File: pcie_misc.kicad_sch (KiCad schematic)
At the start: 0 parts

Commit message: [#57056] Add PCIe circuitry
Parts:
- added C53: C_22u_0603, antmicro-footprints:C_0603_1608Metric, symbol antmicroCapacitors0603:C_22u_0603
- added C54, C55, C56, C57, C58, C60: C_100n_0402, antmicro-footprints:C_0402_1005Metric, symbol antmicroCapacitors0402:C_100n_0402
- added C59: C_68n_0402, antmicro-footprints:C_0402_1005Metric, symbol antmicroCapacitors0402:C_68n_0402
- added R35, R36, R37, R38, R39, R40, R41, R42, R43, R44, R45, R46: R_0R_0402, antmicro-footprints:R_0402_1005Metric, symbol antmicroResistors0402:R_0R_0402
- added R47, R48, R49, R50, R51, R52, R53, R54, R55, R56, R57: R_1k_0402, antmicro-footprints:R_0402_1005Metric, symbol antmicroResistors0402:R_1k_0402
- added TP1, TP2, TP3, TP4: TP_0.75mm_SMD, antmicro-footprints:TP_SMD_0.75mm, symbol antmicroTestPoints:TP_0.75mm_SMD
- added U1: 9DBL0651CKILF, antmicro-footprints:UQFN-40-1EP_5x5mm_P0.4mm_EP3.8x3.8mm, symbol antmicroClockTimingClockGeneratorsPLLsFrequencySynthesizers:9DBL0651CKILF
- added U2: 74AUP2G132, antmicro-footprints:VSSOP-8_2.3x2mm_P0.5mm, symbol antmicroLogicGatesandInverters:74AUP2G132
- added U3: TPS3840PL30DBVR, antmicro-footprints:SOT-23-5, symbol antmicroPMICPowerSequencers:TPS3840PL30DBVR
- added Y1: Oscillator_32.768kHz_ECS_2520MV, antmicro-footprints:Oscillator_SMD_ECS_2520MV_2.5x2mm, symbol antmicroOscillators:Oscillator_32.768kHz_ECS_2520MV
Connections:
- new net: C59.2, C60.2, U3.5 (CT)
- new net: R52.1, U1.38 (~{OE5})
- new net: R56.1, Y1.1 (EN)
- new net: R54.2, R55.1, U1.2 (~{HIBW_BYPM_LOBW})
- new net: R47.1, U1.13 (~{OE0})
- new net: TP4.1, U3.4 (~{MR})
- new net: R50.1, U1.29 (~{OE3})
- new net: R48.1, U1.21 (~{OE1})
- new net: TP3.1, U1.1 (SADR_{TRI})
- new net: TP2.1, U1.10 (SDAT)
- new net: R49.1, U1.24 (~{OE2})
- new net: R51.1, U1.35 (~{OE4})
- new net: R53.1, U1.40 (~{CKPWRGD_PD})
- new net: TP1.1, U1.9 (SCLK)
- new net: U2.1 (1A), U2.2 (1B), Y1.3 (OUT)
- new net +3V3: C53.2, C54.2, C55.2, C56.2, C57.2, C58.2, R52.2, R53.2, R54.1, R56.2, R57.2, U1.11 (VDDDIG3V3), U1.12 (VDDIO), U1.16 (VDD3V3), U1.17 (VDDIO), U1.25 (VDDA3V3), U1.26 (VDDIO), U1.31 (VDD3V3), U1.32 (VDDIO), U1.39 (VDDIO), U1.5 (VDDR), U2.8 (VCC), U3.2 (VDD), Y1.4 (VDD)
- new net DIF0+: R35.1, U1.14 (DIF0+)
- new net DIF0-: R36.1, U1.15 (DIF0-)
- new net DIF1+: R37.1, U1.18 (DIF1+)
- new net DIF1-: R38.1, U1.19 (DIF1-)
- new net DIF2+: R39.1, U1.22 (DIF2+)
- new net DIF2-: R40.1, U1.23 (DIF2-)
- new net DIF3+: R41.1, U1.27 (DIF3+)
- new net DIF3-: R42.1, U1.28 (DIF3-)
- new net DIF4+: R43.1, U1.33 (DIF4+)
- new net DIF4-: R44.1, U1.34 (DIF4-)
- new net DIF5+: R45.1, U1.36 (DIF5+)
- new net DIF5-: R46.1, U1.37 (DIF5-)
- new net GND: C53.1, C54.1, C55.1, C56.1, C57.1, C58.1, C59.1, C60.1, R47.2, R48.2, R49.2, R50.2, R51.2, R55.2, U1.41 (EPAD), U1.8 (GNDDIG), U2.4 (GND), U2.5 (2A), U2.6 (2B), U3.3 (GND), Y1.2 (GND)
- new net PCIE_{REF0}.CK+: R35.2
- new net PCIE_{REF0}.CK-: R36.2
- new net PCIE_{REF1}.CK+: R37.2
- new net PCIE_{REF1}.CK-: R38.2
- new net PCIE_{REF2}.CK+: R39.2
- new net PCIE_{REF2}.CK-: R40.2
- new net PCIE_{REF3}.CK+: R41.2
- new net PCIE_{REF3}.CK-: R42.2
- new net PCIE_{REF4}.CK+: R43.2
- new net PCIE_{REF4}.CK-: R44.2
- new net PCIE_{REFIN}.CK+: U1.6 (CLK_IN+)
- new net PCIE_{REFIN}.CK-: U1.7 (CLK_IN-)
- new net SUSCLK: U2.7 (1Y)
- new net ~{PERST}: R57.1, U3.1 (~{RESET})
- no-connect marks 0 -> 3
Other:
- note added: "100 ms delay"
- note added: "PCIe CLOCK FANOUT BUFFER"
- note added: "SUSCLK generator"
- note added: "~{PERST} generator"
- company: (none) -> Antmicro Ltd.
- title: (none) -> Com Express 7 baseboard

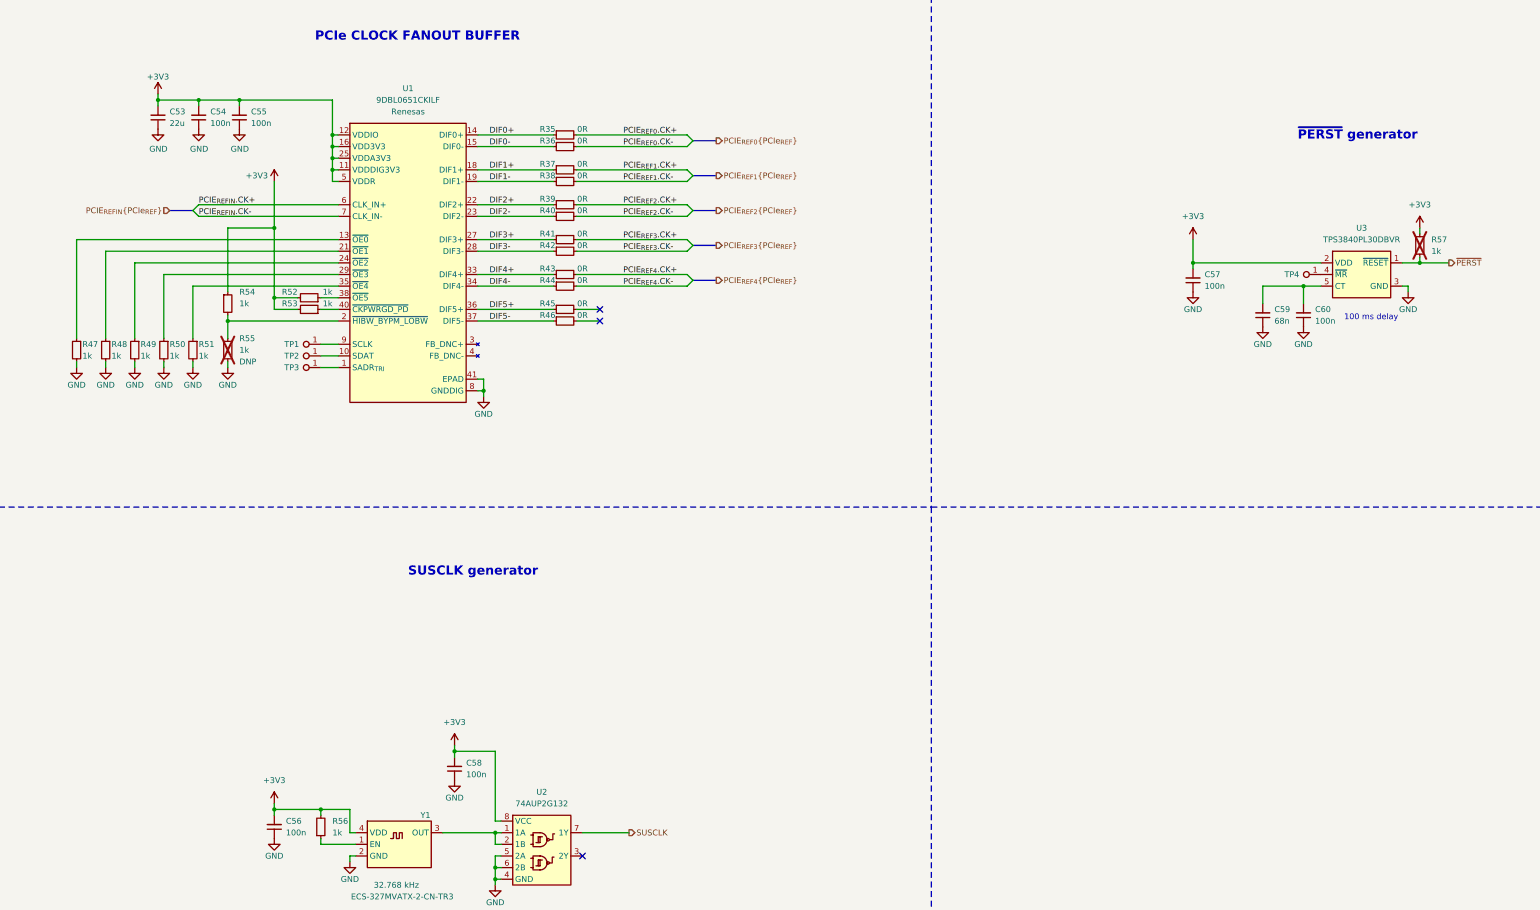
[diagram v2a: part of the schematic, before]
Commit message: [#58137] Update backplane connector pinout
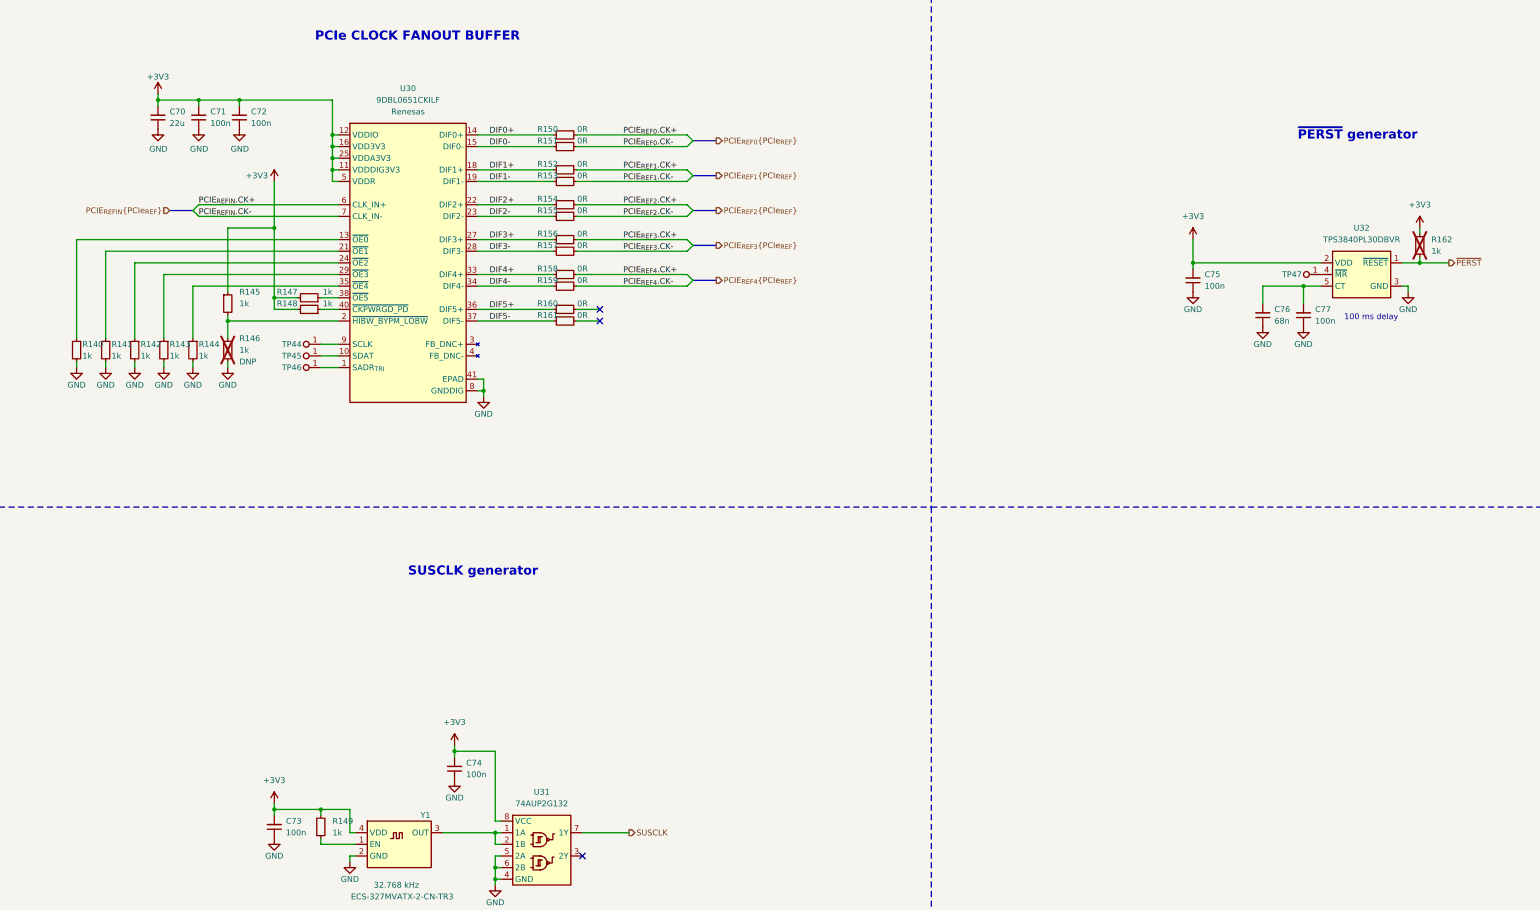
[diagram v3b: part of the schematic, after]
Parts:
- renumbered C53 to C70, C54 to C71, C55 to C72, C56 to C73, C58 to C74, C57 to C75, C59 to C76, C60 to C77, R47 to R140, R48 to R141, R49 to R142, R50 to R143, R51 to R144, R54 to R145, R55 to R146, R52 to R147, R53 to R148, R56 to R149, R35 to R150, R36 to R151, R37 to R152, R38 to R153, R39 to R154, R40 to R155, R41 to R156, R42 to R157, R43 to R158, R44 to R159, R45 to R160, R46 to R161, R57 to R162, TP1 to TP44, TP2 to TP45, TP3 to TP46, TP4 to TP47, U1 to U30, U2 to U31, U3 to U32

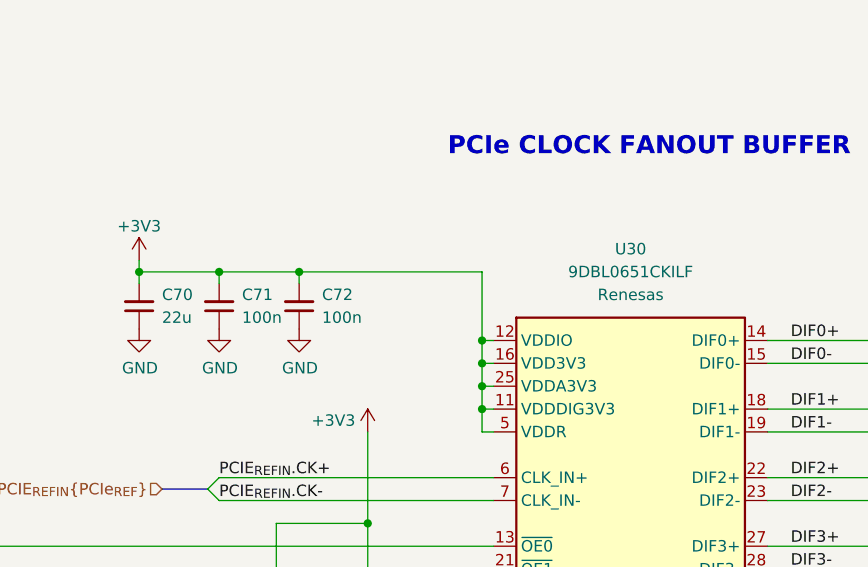
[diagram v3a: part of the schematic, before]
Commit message: [#58137] Add DC/DC supplies
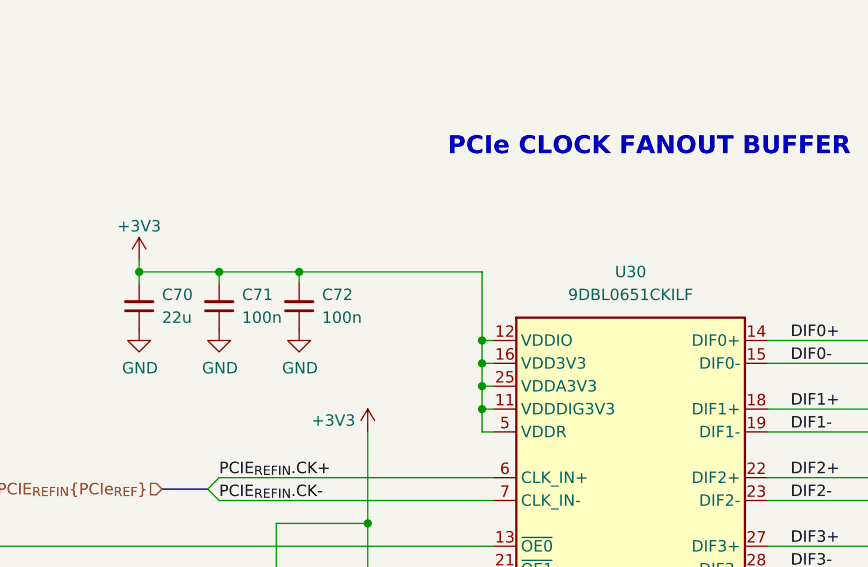
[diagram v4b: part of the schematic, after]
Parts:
- C70: value C_22u_0603 -> C_22u_16V_0603; symbol antmicroCapacitors0603:C_22u_0603 -> antmicroCapacitors0603:C_22u_16V_0603; MPN GRM188R60J226MEA0D -> CL10A226MO7JZNC; Manufacturer Murata -> Samsung Electro-Mechanics; Voltage (none) -> 16V
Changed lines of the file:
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@@
     )
   )
-  (symbol (lib_id "antmicroCapacitors0603:C_22u_0603") (at 49.53 52.07 90) (unit 1)
+  (symbol (lib_id "antmicroCapacitors0603:C_22u_16V_0603") (at 49.53 52.07 90) (unit 1)
     (in_bom yes) (on_board yes) (dnp no) (fields_autoplaced)
-    (property "Reference" "C70" (at 52.07 48.2536 90)
+    (property "Reference" "C70" (at 52.07 48.2535 90)
       (effects (font (size 1.27 1.27) (thickness 0.15)) (justify right))
     )
-    (property "Value" "C_22u_0603" (at 59.69 31.75 0)
+    (property "Value" "C_22u_16V_0603" (at 59.69 31.75 0)
       (effects (font (size 1.27 1.27) (thickness 0.15)) (justify left bottom) hide)
     )
@@
       (effects (font (size 1.27 1.27) (thickness 0.15)) (justify left bottom) hide)
     )
-    (property "Datasheet" "https://www.murata.com/products/productdetail?partno=GRM188R60J226MEA0%23" (at 64.77 31.75 0)
-      (effects (font (size 1.27 1.27) (thickness 0.15)) (justify left bottom) hide)
-    )
-    (property "MPN" "GRM188R60J226MEA0D" (at 67.31 31.75 0)
-      (effects (font (size 1.27 1.27) (thickness 0.15)) (justify left bottom) hide)
-    )
-    (property "Manufacturer" "Murata" (at 69.85 31.75 0)
+    (property "Datasheet" "https://product.samsungsem.com/mlcc/CL10A226MO7JZN.do" (at 64.77 31.75 0)
+      (effects (font (size 1.27 1.27) (thickness 0.15)) (justify left bottom) hide)
+    )
+    (property "MPN" "CL10A226MO7JZNC" (at 67.31 31.75 0)
+      (effects (font (size 1.27 1.27) (thickness 0.15)) (justify left bottom) hide)
+    )
+    (property "Manufacturer" "Samsung Electro-Mechanics" (at 69.85 31.75 0)
       (effects (font (size 1.27 1.27) (thickness 0.15)) (justify left bottom) hide)
     )
@@
       (effects (font (size 1.27 1.27) (thickness 0.15)) (justify left bottom) hide)
     )
-    (property "Val" "22u" (at 52.07 50.7936 90)
+    (property "Val" "22u" (at 52.07 50.7935 90)
       (effects (font (size 1.27 1.27) (thickness 0.15)) (justify right))
     )
-    (property "Voltage" "" (at 77.47 31.75 0)
+    (property "Voltage" "16V" (at 77.47 31.75 0)
       (effects (font (size 1.27 1.27)) (justify left bottom) hide)
     )
@@
   (symbol (lib_id "antmicroClockTimingClockGeneratorsPLLsFrequencySynthesizers:9DBL0651CKILF") (at 88.9 53.34 0) (unit 1)
     (in_bom yes) (on_board yes) (dnp no) (fields_autoplaced)
-    (property "Reference" "U30" (at 104.14 43.18 0)
+    (property "Reference" "U30" (at 104.14 45.72 0)
       (effects (font (size 1.27 1.27) (thickness 0.15)))
     )
@@
       (effects (font (size 1.27 1.27) (thickness 0.15)) (justify left bottom) hide)
     )
-    (property "MPN" "9DBL0651CKILF" (at 104.14 45.72 0)
+    (property "MPN" "9DBL0651CKILF" (at 104.14 48.26 0)
       (effects (font (size 1.27 1.27) (thickness 0.15)))
     )
     (property "Manufacturer" "Renesas" (at 104.14 48.26 0)
-      (effects (font (size 1.27 1.27) (thickness 0.15)))
+      (effects (font (size 1.27 1.27) (thickness 0.15)) hide)
     )
     (property "Author" "Antmicro" (at 134.62 71.12 0)

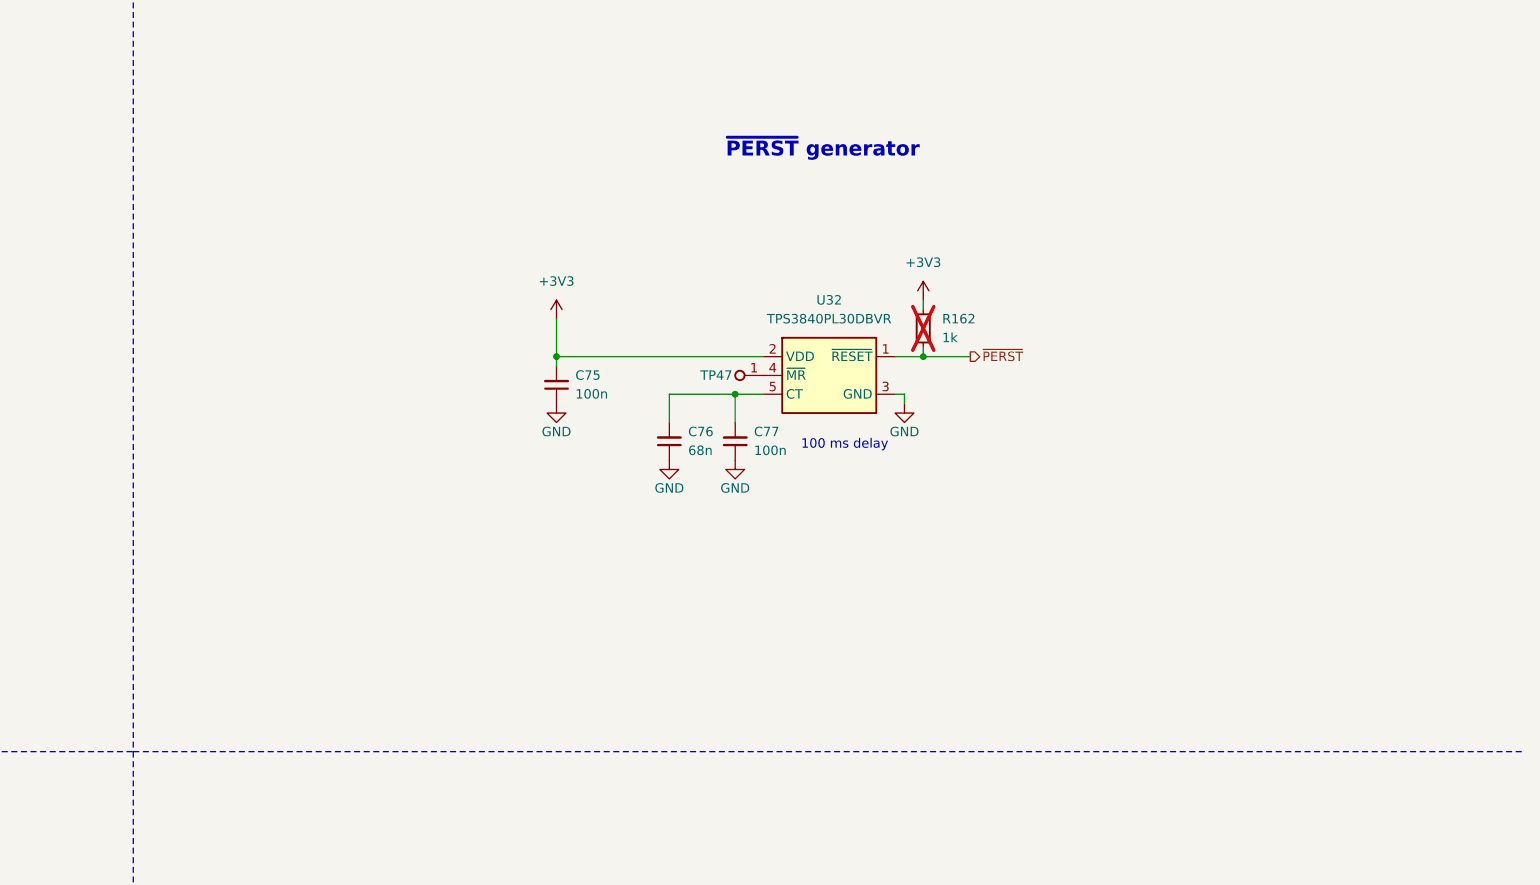
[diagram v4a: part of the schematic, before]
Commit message: [#58137] Add power sequencing and reset
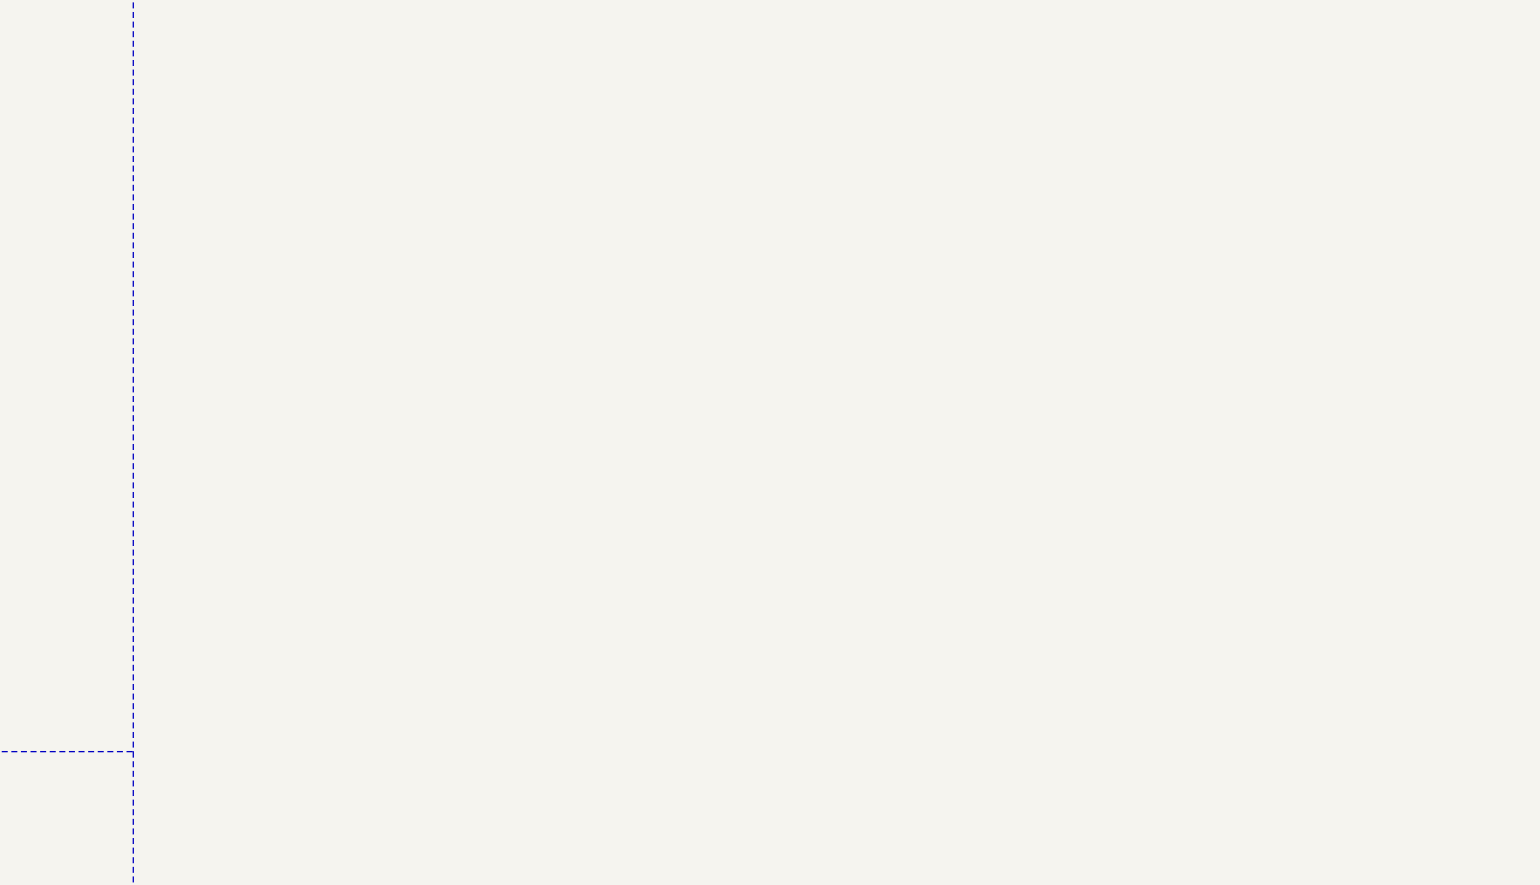
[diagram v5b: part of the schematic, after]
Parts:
- removed C75, C77: C_100n_0402, antmicro-footprints:C_0402_1005Metric, symbol antmicroCapacitors0402:C_100n_0402
- removed C76: C_68n_0402, antmicro-footprints:C_0402_1005Metric, symbol antmicroCapacitors0402:C_68n_0402
- removed R162: R_1k_0402, antmicro-footprints:R_0402_1005Metric, symbol antmicroResistors0402:R_1k_0402
- removed TP47: TP_0.75mm_SMD, antmicro-footprints:TP_SMD_0.75mm, symbol antmicroTestPoints:TP_0.75mm_SMD
- removed U32: TPS3840PL30DBVR, antmicro-footprints:SOT-23-5, symbol antmicroPMICPowerSequencers:TPS3840PL30DBVR
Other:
- note removed: "100 ms delay"
- note removed: "~{PERST} generator"
